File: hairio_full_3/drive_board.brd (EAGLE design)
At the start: 58 x 49 mm, 29 parts, among them J1 105313-1104, J2 105313-1104, P1 S2B-PH-SM4-TB(LF)(SN), P2 S2B-PH-SM4-TB(LF)(SN)

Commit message: update board
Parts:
- moved R7 4.07 mm to (33.1, 60.7)
- moved R11 3.18 mm to (33.1, 64.1)
- moved L1 2.22 mm to (68.2, 65.5), turned to 270 degrees
- moved C2 1.65 mm to (52.1, 63.1)
- moved BLE 0.64 mm to (44.5, 73.0)
- moved NPN4 0.52 mm to (82.7, 45.8)
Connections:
- net A0: now also ARDUINO_NANO1.7; no longer ARDUINO_NANO1.4
- net A1_THERM_1: now also ARDUINO_NANO1.4; no longer ARDUINO_NANO1.5
- net A2_THERM_2: now also ARDUINO_NANO1.5; no longer ARDUINO_NANO1.6
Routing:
- net DRIVE_SIGNAL_2: track 34.2 -> 2.54 mm
- net NANO_5V_OUT: track 58.3 -> 76.4 mm
- net A2_THERM_2: track 58.2 -> 65.8 mm
- net N$10: track 24.4 -> 17.1 mm
- net CAPTOUCH_1: track 45.4 -> 50.0 mm
- net A0: track 29.2 -> 32.6 mm
- net N$13: track 38.4 -> 35.8 mm
- net GND: track 45.6 -> 47.6 mm
- net D4_BT_RX1: track 17.2 -> 15.4 mm
- net N$5: track 22.3 -> 20.4 mm
- net DRIVE_SIGNAL_1: track 60.4 -> 59.1 mm
- net CAPTOUCH_2: track 65.8 -> 64.9 mm
- net D5: track 7.60 -> 8.49 mm
- net N$6: track 12.8 -> 12.1 mm
- net D12_BT_MODE: track 3.81 -> 4.45 mm
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
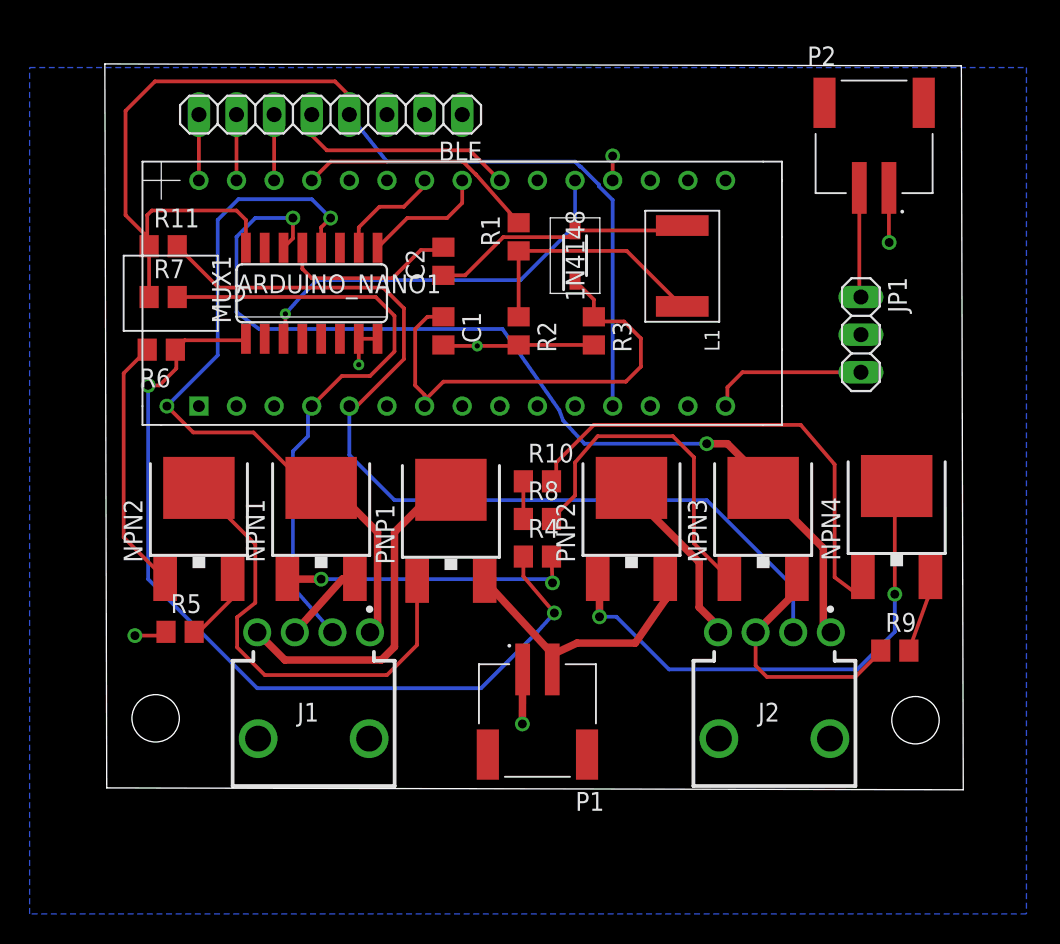
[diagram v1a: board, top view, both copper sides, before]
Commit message: hairio board with no routes between header pins
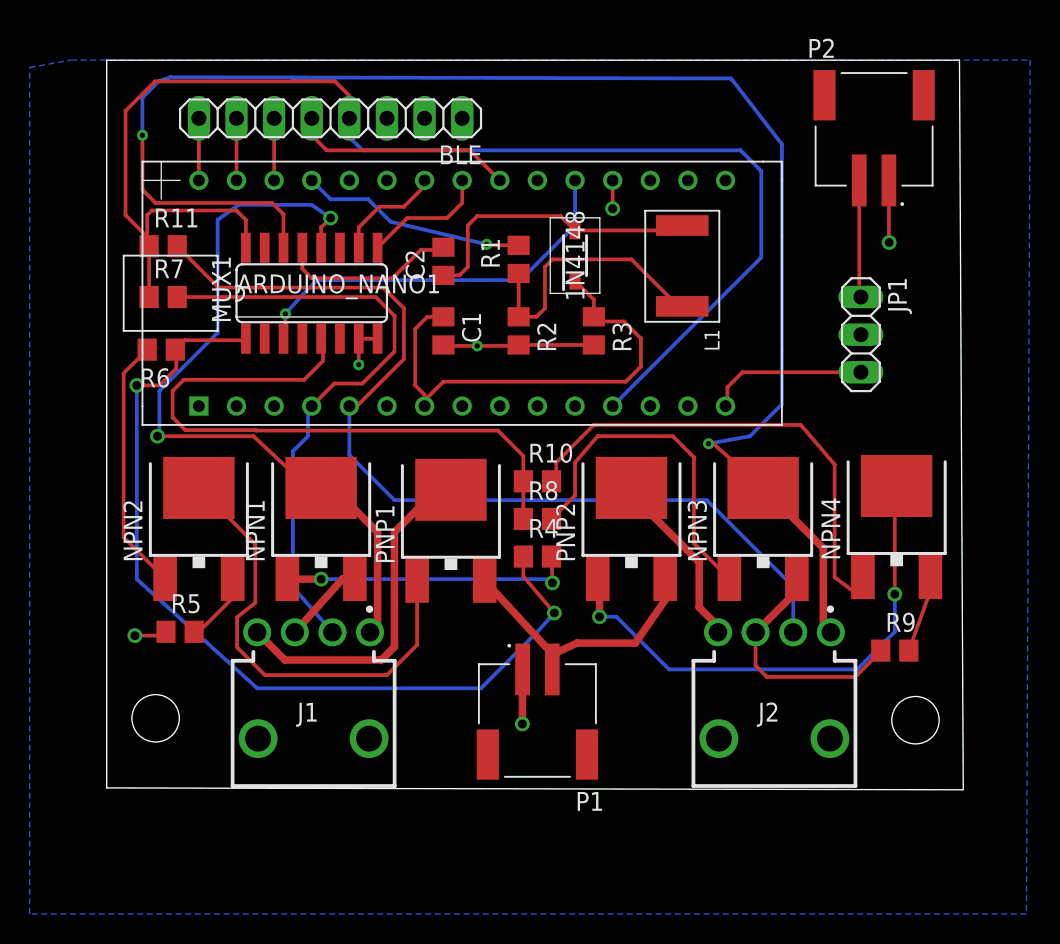
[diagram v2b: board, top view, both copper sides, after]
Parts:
- moved R1 1.52 mm to (57.1, 63.2)
- moved P2 0.51 mm to (81.2, 68.6)
- moved BLE 0.25 mm to (44.5, 72.8)
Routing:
- net DRIVE_SIGNAL_2: track 2.54 -> 43.4 mm
- net CAPTOUCH_2: track 64.9 -> 104.5 mm
- net NANO_5V_OUT: track 76.4 -> 92.2 mm
- net N$7: track 17.5 -> 20.0 mm
- net CAPTOUCH_1: track 50.0 -> 51.5 mm
- net N$10: track 17.1 -> 18.5 mm
- net DRIVE_SIGNAL_1: track 59.1 -> 60.4 mm
- net N$9: track 16.3 -> 15.3 mm, vias 0 -> 1
- net GND: track 47.6 -> 48.4 mm
- net N$16: track 7.41 -> 7.92 mm
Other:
- board size 58 x 49 mm -> 57.8 x 49.3 mm

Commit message: change via size and shift trace
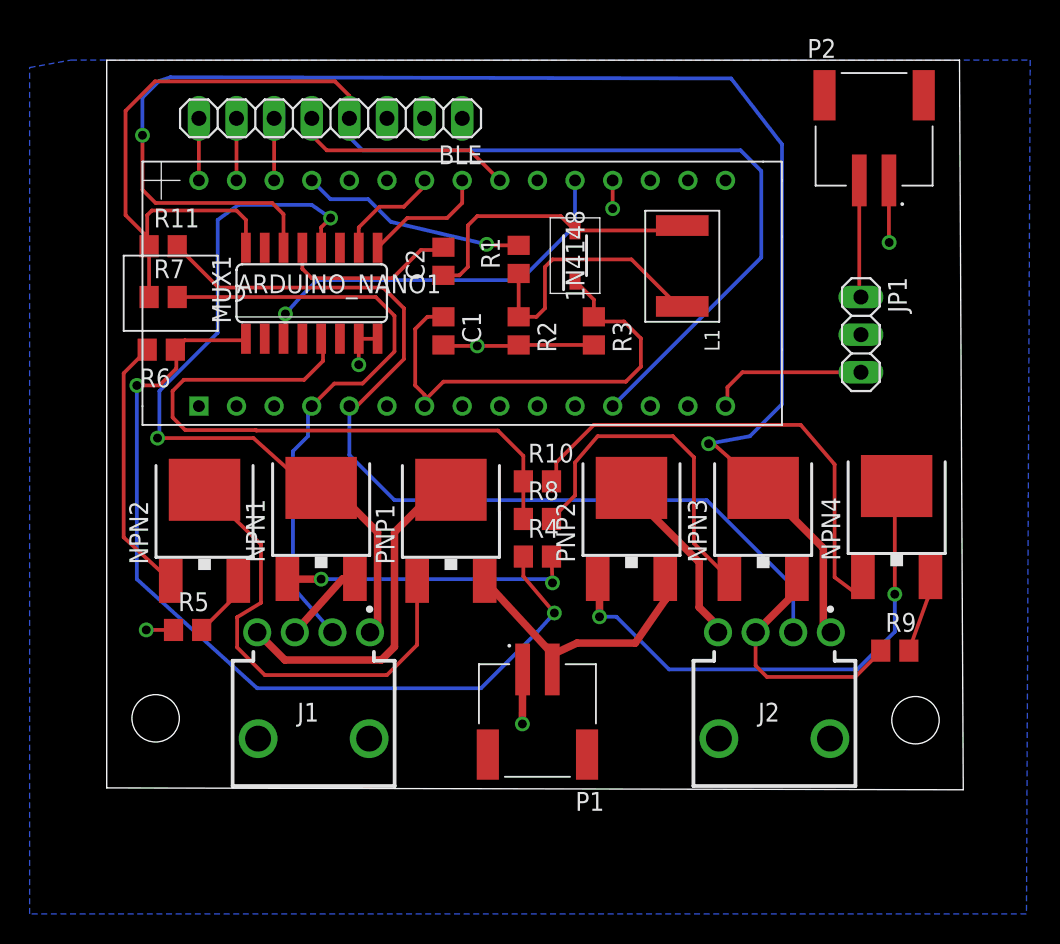
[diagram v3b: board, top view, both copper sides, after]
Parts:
- moved R5 0.52 mm to (34.8, 38.2)
- moved NPN2 0.40 mm to (35.9, 45.6)

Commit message: More tweaks to board
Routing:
- net NANO_5V_OUT: track 92.2 -> 90.9 mm
- net N$1: track 17.7 -> 18.2 mm
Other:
- board size 57.8 x 49.3 mm -> 58.3 x 49.3 mm

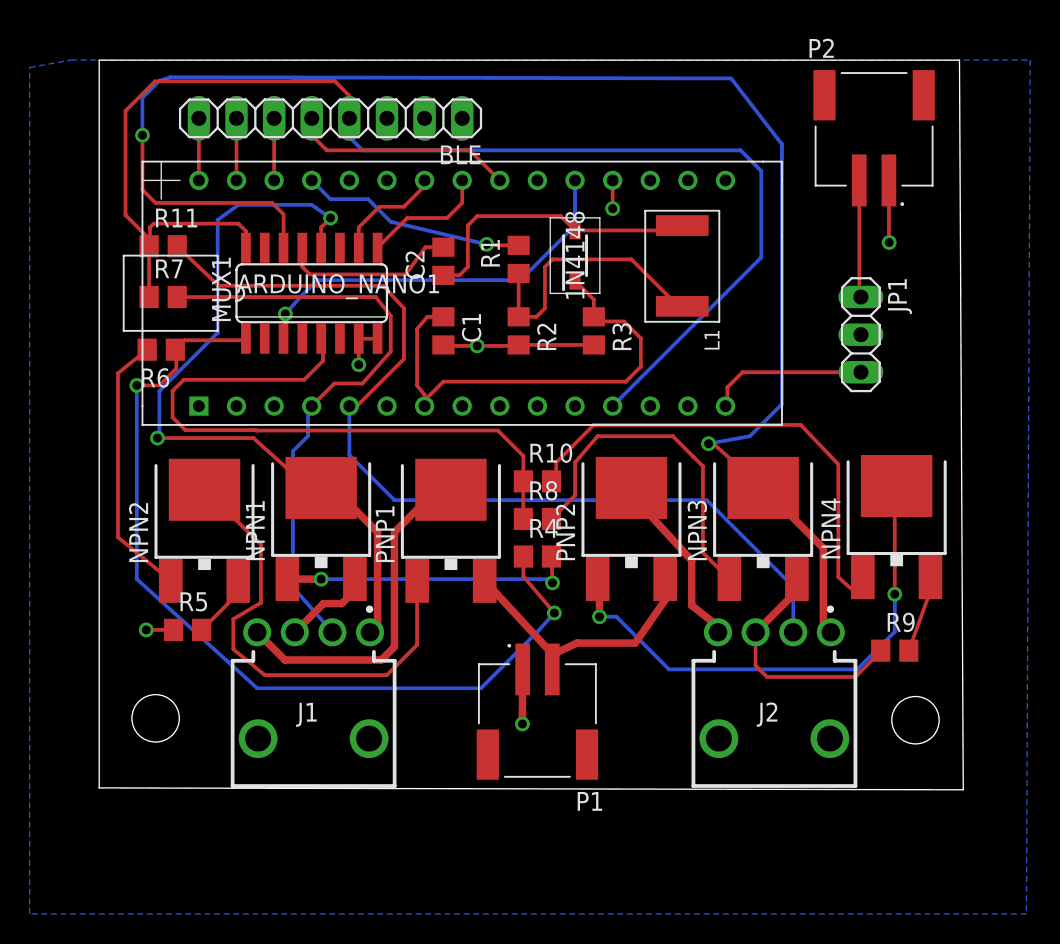
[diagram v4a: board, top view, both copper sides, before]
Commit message: new board -- the dimensioned version of what got made for demos (with ground plane fix after accidental deletion)
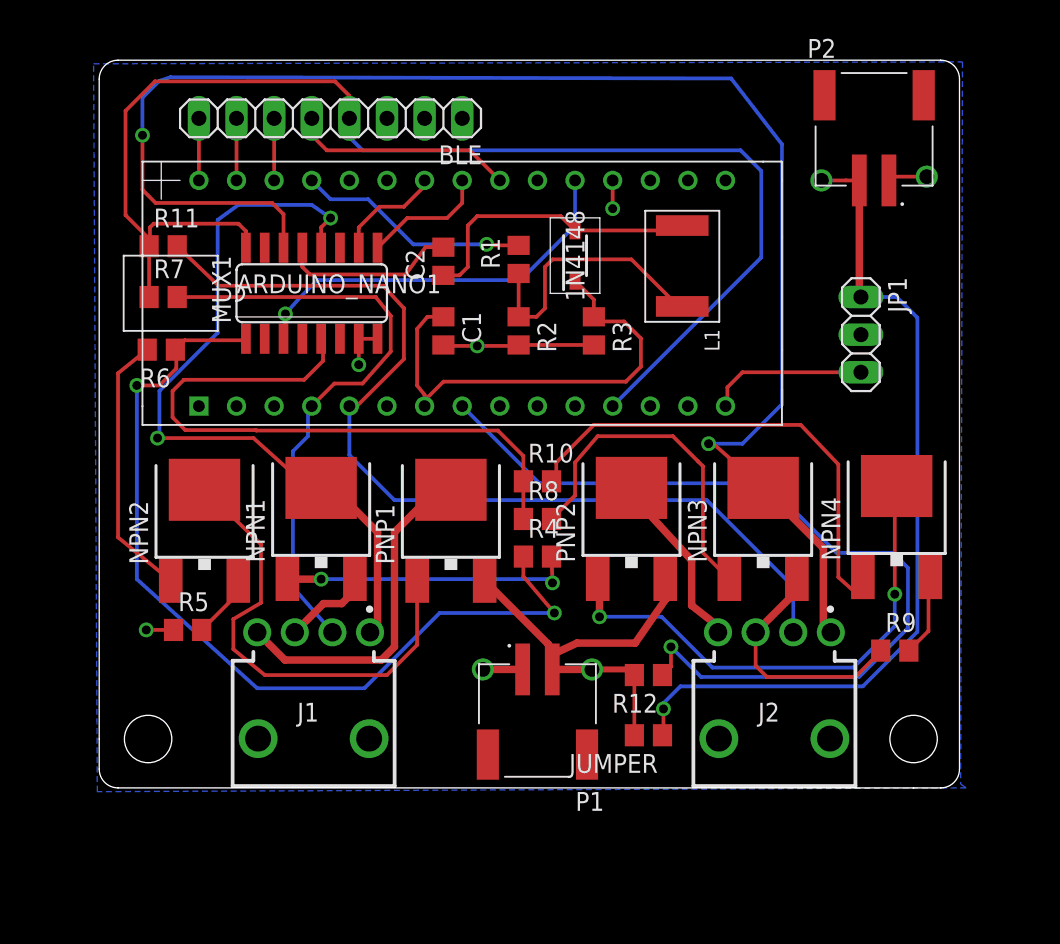
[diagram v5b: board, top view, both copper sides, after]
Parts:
- added JUMPER: (no value), resistor:R0805
- added R12: 4.7K, resistor:R0805
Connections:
- new net V_DRIVE_MONITOR: ARDUINO_NANO1.8, R12.1
- net N$16: now also JUMPER.1
- net PWR: now also JUMPER.2, R12.2
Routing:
- net V_DRIVE_MONITOR: track 0.00 -> 59.7 mm, vias 0 -> 1
- net N$16: track 7.92 -> 58.3 mm, vias 0 -> 2
- net PWR: track 19.9 -> 29.1 mm, vias 0 -> 1
- net GND: track 48.3 -> 45.3 mm
- net CAPTOUCH_2: track 104.5 -> 105.5 mm
- net N$14: track 23.3 -> 24.3 mm
- added copper zone on layer 16, net N$20
- removed copper zone on layer 16, net GND
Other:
- board size 58.3 x 49.3 mm -> 58.1 x 49.1 mm

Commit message: board layout with dimensions -- modified post fabrication
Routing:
- added copper zone on layer 16, net GND
- removed copper zone on layer 16, net N$20
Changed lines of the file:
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@@
 <wire x1="82.407" y1="68.834" x2="84.709" y2="68.834" width="0.254" layer="1"/>
 <via x="84.709" y="68.834" extent="1-16" drill="1"/>
-<wire x1="63.5" y1="68.58" x2="82.153" y2="68.58" width="0" layer="19" extent="1-1"/>
-<wire x1="62.23" y1="57.47" x2="63.5" y2="66.675" width="0" layer="19" extent="1-1"/>
-<wire x1="47.625" y1="57.8866" x2="52.07" y2="57.47" width="0" layer="19" extent="1-1"/>
-<wire x1="68.58" y1="53.34" x2="62.23" y2="57.47" width="0" layer="19" extent="1-1"/>
-<wire x1="50.8" y1="72.771" x2="63.5" y2="68.58" width="0" layer="19" extent="1-1"/>
-<wire x1="75.94" y1="41.68" x2="68.58" y2="53.34" width="0" layer="19" extent="1-1"/>
-<wire x1="46.095" y1="41.68" x2="46.355" y2="56.134" width="0" layer="19" extent="1-1"/>
-<wire x1="33.848" y1="38.227" x2="42.037" y2="38.066" width="0" layer="19" extent="1-1"/>
-<wire x1="54.737" y1="35.56" x2="46.095" y2="40.888" width="0" layer="19" extent="1-1"/>
+<polygon width="0.254" layer="16">
+<vertex x="87.122" y="76.581"/>
+<vertex x="86.995" y="27.813"/>
+<vertex x="87.376" y="27.559"/>
+<vertex x="28.702" y="27.305"/>
+<vertex x="28.448" y="76.454"/>
+</polygon>
 </signal>
 <signal name="N$1">
@@
 <signal name="N$24">
 </signal>
-<signal name="N$20">
-<polygon width="0.254" layer="16">
-<vertex x="87.122" y="76.581"/>
-<vertex x="86.995" y="27.813"/>
-<vertex x="87.376" y="27.559"/>
-<vertex x="28.702" y="27.305"/>
-<vertex x="28.448" y="76.454"/>
-</polygon>
-</signal>
 </signals>
